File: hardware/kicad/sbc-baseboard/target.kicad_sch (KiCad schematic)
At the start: 30 parts, among them J13 Console VREF/TXD/RXD/GND, J14 +5V_TGT out, J15 GPIO + I2C breakout, U701 TXB0104PW, U702 TXB0108PW, U703 TXS0102DCU, U704 TPS26630RGE

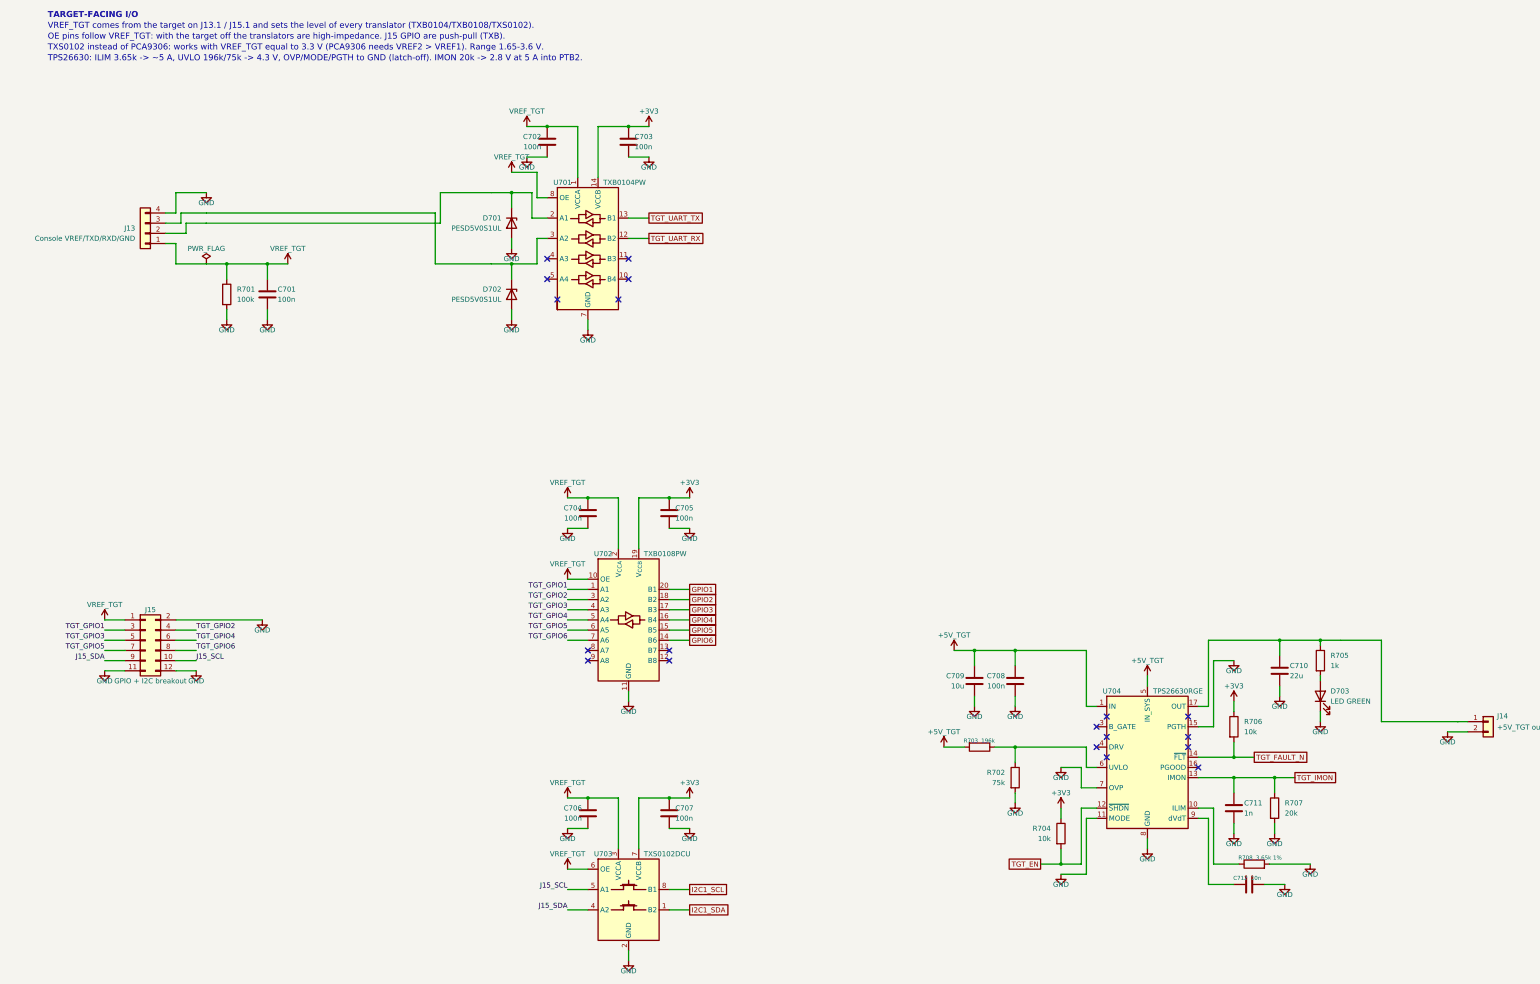
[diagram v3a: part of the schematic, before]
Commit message: Symbol name clearance, divider at the reading pin, inlet TVS orientation
Symbols: a top or bottom pin's name runs vertically into the body, so box
symbols now grow outward by whole rows wherever such a name would reach a
side pin's name (USB2517 three rows on top, K64 two rows top and bottom,
PCA9517A three rows on top); the side-pin rows stay where they were so the
sheet layouts are unaffected. U402's VDD names no longer print over USBUP_DP.

Frame pass: nothing on the sheet frame or the title block, enforced by the
layout gate (usable area 15..405 x 15..282 mm, title block from 300/253).

Flow pass: pull-ups hang up to their rail, pull-downs hang down (R408/R409
and the other strap and sense resistors). The J1 VBUS_DET divider sits at
U402 pin 44, the pin that reads it; J1's VBUS lane is a plain stretch that
U401 taps; J1 and U401 lifted clear of the hub's +3V3 bus. The hub's left
strap lanes turn in columns starting at x = 118.11 so they clear the bottom
decoupling ladders (fan() grew a turn_at argument for this).

Inlet TVS D102 hangs from J2's VBUS lane as a D_Zener with its cathode on
VBUS_IN. At 8579cd2 it was drawn with the bidirectional D_TVS symbol and
pad 1 (the SMA cathode) on GND, which would have forward-biased it.

Bucks: the FB pulls start past the catch diode's text; the two notes are
rewrapped and sit between U101 and the compensation parts.

Gates on every sheet: ERC 0, endpoint contacts 0, rail merges 0, frame 0,
no text on bodies or wires. Connectivity identical to 8579cd2 (symmetric
passives order-free) except the TVS orientation.

Co-Authored-By: Claude Fable 5.1 <noreply@anthropic.com>
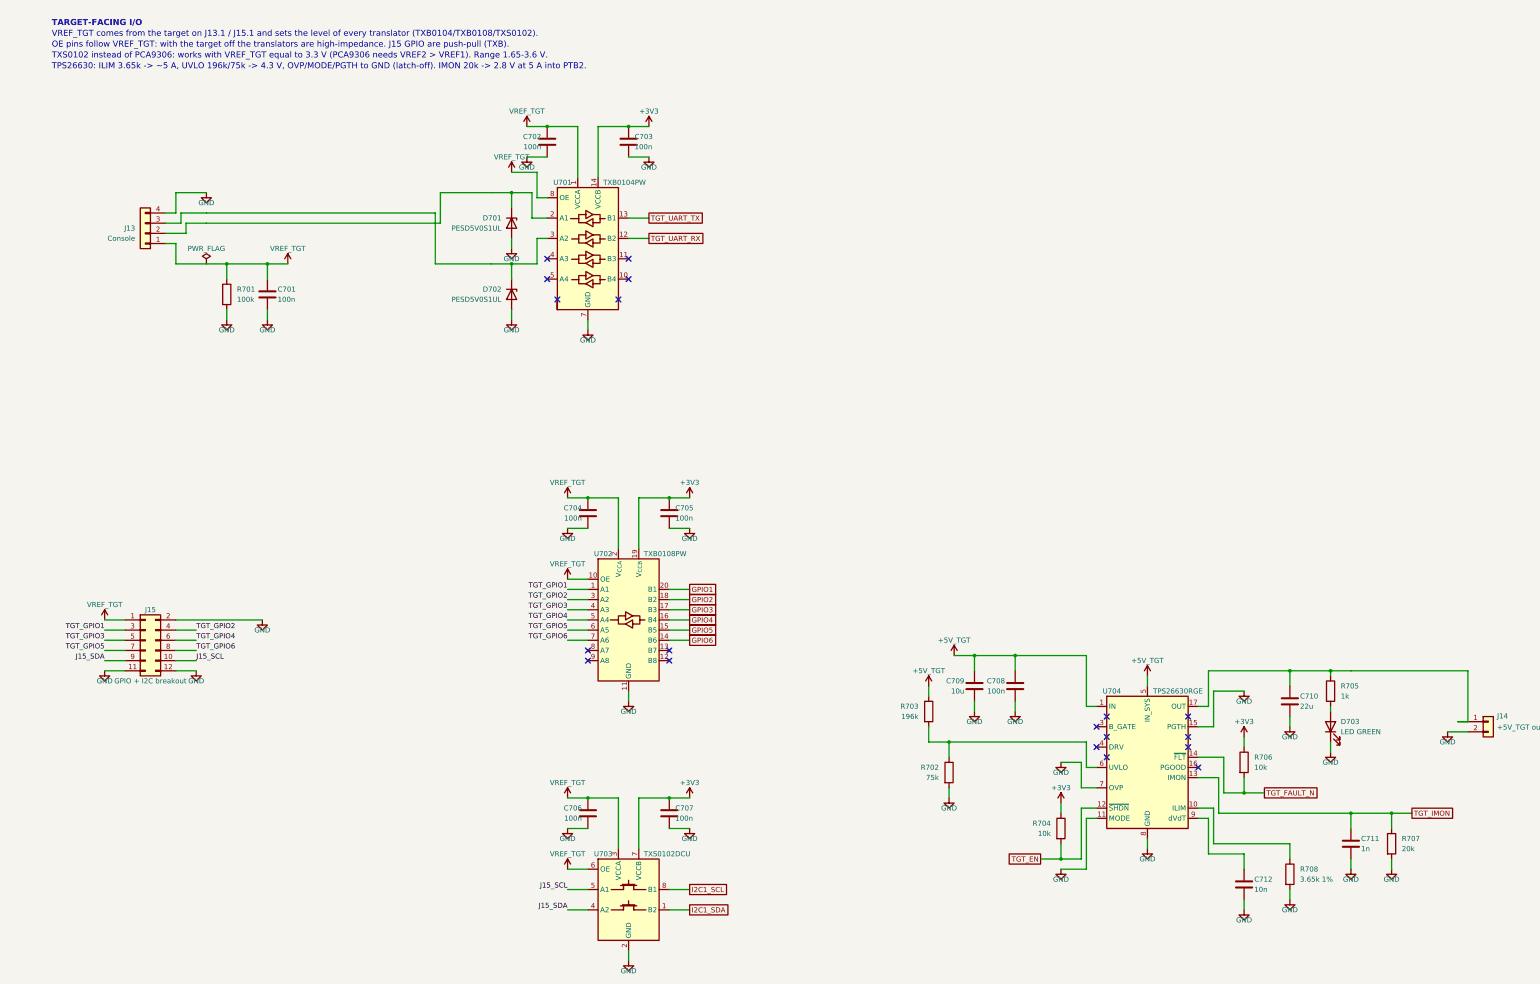
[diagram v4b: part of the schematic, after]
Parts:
- J13: value Console VREF/TXD/RXD/GND -> Console
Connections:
- net +5V_TGT: now also R703.1; no longer R703.2
- net at R702.1, U704.6 (UVLO): now also R703.2; no longer R703.1

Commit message: Reference-design review; pin numbers and real text widths in the layout gate
Review (docs/reference-design-review.md): every IC's surrounding parts
compared with its datasheet typical application or evaluation board.
Brought in line:
- TPS54560B compensation 16.9k / 4.7 nF / 47 pF (the 5 V / 400 kHz design
  example, same 141 uF ceramic output); the placeholders are gone.
- TPS62823 divider 453k / 100k with the 120 pF feed-forward capacitor the
  datasheet recommends.
- USB2517 VBUS_DET from the EVB: 100k / 100k with 1 uF (was 10k / 22k, 3.4 V
  at a 3.3 V pin).
- KSZ8081 MDIO pull-up 1.0k as the datasheet requires (was 4.7k).
- FT231X: 27 R in series and 47 pF on USBDM/USBDP, datasheet figure 6.1.
Deviations kept and documented: the bucks' EN gated by the PD controller
instead of a UVLO divider, the FT231X fed by a power switch instead of a
ferrite bead, translator OE tied to the target rail.

Layout gate: pin numbers are text boxes like any other, and all text widths
come from a per-glyph table fitted to the extents KiCad writes into its PDF
(check_pins.py); the generator's spacing uses the same table. That exposed
and fixed: reference/value overlaps on narrow symbols (now stacked), rail
names printed over each other (the lane end and hanging pull-up now carry
half the rail name), a port-switch value over its pin number, turned parts
with text on the pin side, lane stacks whose spread collapsed at the grid
snap, routes landing on connector pin stubs (J16, J601, J14, D202 moved),
the PD controller's I2C and gate routes that crossed half the sheet (now
labels), and the port /FAULT and I2C1 pull-ups, which as hanging resistors
staggered off the sheet and are now one column to one +3V3 symbol. The
port switch carries FAULT above OUT so the switched rail's parts hang below
the label; the VBUS row is drawn from the connector back to the switch.

All sheets: ERC 0, contacts 0, merges 0, layout 0 in every category.
Connectivity against 8579cd2 differs only in the value ch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
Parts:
- J15: value GPIO + I2C breakout -> GPIO + I2C
